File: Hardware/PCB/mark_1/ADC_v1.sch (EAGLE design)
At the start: 1 part, among them Q1 IRLML6402

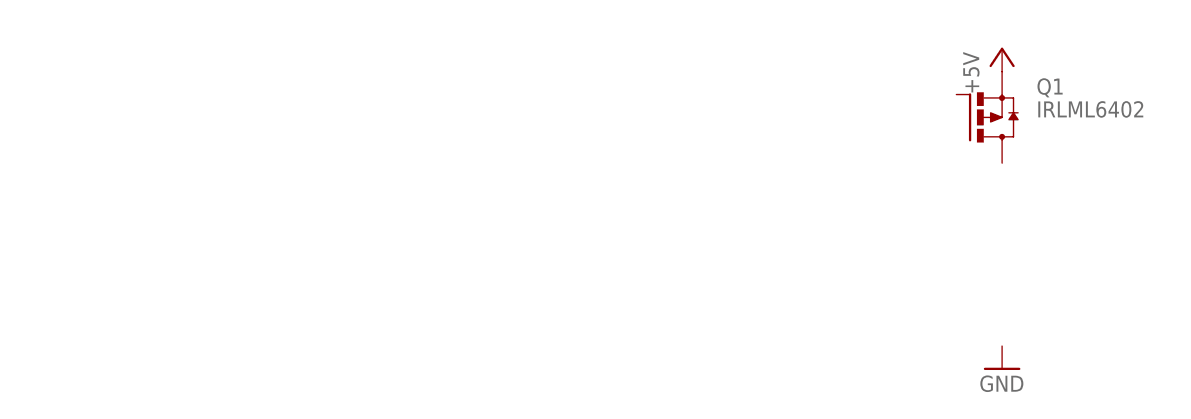
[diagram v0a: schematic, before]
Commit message: 
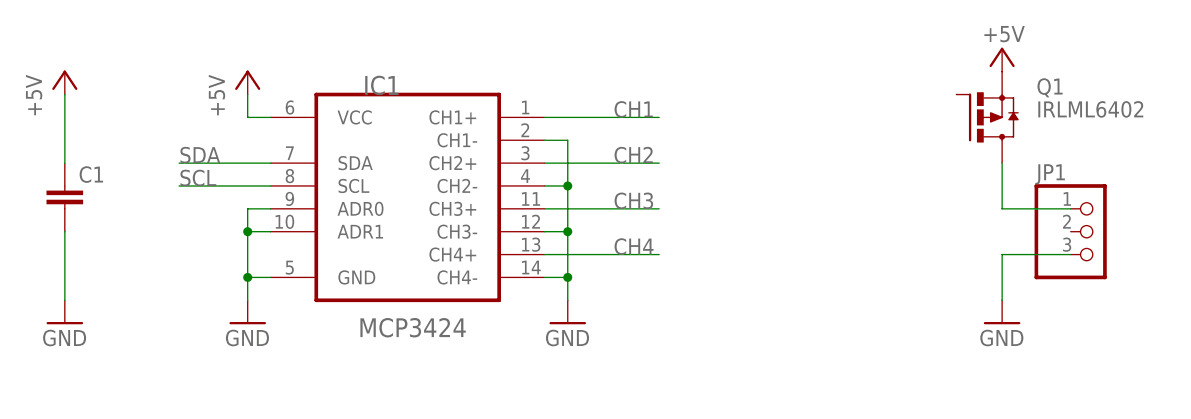
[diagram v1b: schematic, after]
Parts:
- added C1: (no value), mark_1:C-EUC0805K
- added IC1: MCP3424, mark_1:MCP3424
- added JP1: (no value), mark_1:PINHD-1X3180
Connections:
- new net CH1: IC1.CH1+
- new net CH2: IC1.CH2+
- new net CH3: IC1.CH3+
- new net CH4: IC1.CH4+
- new net GND: C1.2, IC1.ADR0, IC1.ADR1, IC1.CH1-, IC1.CH2-, IC1.CH3-, IC1.CH4-, IC1.GND, JP1.3
- new net N$1: JP1.1, Q1.D
- new net SCL: IC1.SCL
- new net SDA: IC1.SDA
- net +5V: now also C1.1, IC1.VCC
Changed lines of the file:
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@@
 <part name="P+1" library="mark_1" deviceset="+5V" device=""/>
 <part name="GND1" library="mark_1" deviceset="GND" device=""/>
+<part name="IC1" library="mark_1" deviceset="MCP3424" device=""/>
+<part name="P+2" library="mark_1" deviceset="+5V" device=""/>
+<part name="GND2" library="mark_1" deviceset="GND" device=""/>
+<part name="C1" library="mark_1" deviceset="C-EU" device="C0805K"/>
+<part name="P+3" library="mark_1" deviceset="+5V" device=""/>
+<part name="GND3" library="mark_1" deviceset="GND" device=""/>
+<part name="JP1" library="mark_1" deviceset="PINHD-1X3" device="180"/>
+<part name="GND4" library="mark_1" deviceset="GND" device=""/>
 </parts>
 <sheets>
@@
 <instances>
 <instance part="Q1" gate="G$1" x="25.4" y="40.64"/>
-<instance part="P+1" gate="1" x="27.94" y="48.26"/>
-<instance part="GND1" gate="1" x="27.94" y="12.7"/>
+<instance part="P+1" gate="1" x="27.94" y="48.26" smashed="yes">
+<attribute name="VALUE" x="30.48" y="50.8" size="1.778" layer="96" rot="R180"/>
+</instance>
+<instance part="GND1" gate="1" x="-20.32" y="17.78"/>
+<instance part="IC1" gate="A" x="-38.1" y="33.02"/>
+<instance part="P+2" gate="1" x="-55.88" y="45.72"/>
+<instance part="GND2" gate="1" x="-55.88" y="17.78"/>
+<instance part="C1" gate="G$1" x="-76.2" y="33.02"/>
+<instance part="P+3" gate="1" x="-76.2" y="45.72"/>
+<instance part="GND3" gate="1" x="-76.2" y="17.78"/>
+<instance part="JP1" gate="A" x="38.1" y="27.94"/>
+<instance part="GND4" gate="1" x="27.94" y="17.78"/>
 </instances>
 <busses>
@@
 <pinref part="P+1" gate="1" pin="+5V"/>
 </segment>
+<segment>
+<pinref part="IC1" gate="A" pin="VCC"/>
+<pinref part="P+2" gate="1" pin="+5V"/>
+<wire x1="-55.88" y1="43.18" x2="-55.88" y2="40.64" width="0.1524" layer="91"/>
+<wire x1="-55.88" y1="40.64" x2="-53.34" y2="40.64" width="0.1524" layer="91"/>
+</segment>
+<segment>
+<pinref part="C1" gate="G$1" pin="1"/>
+<pinref part="P+3" gate="1" pin="+5V"/>
+<wire x1="-76.2" y1="43.18" x2="-76.2" y2="35.56" width="0.1524" layer="91"/>
+</segment>
 </net>
+<net name="GND" class="0">
+<segment>
+<pinref part="IC1" gate="A" pin="GND"/>
+<pinref part="GND2" gate="1" pin="GND"/>
+<wire x1="-55.88" y1="20.32" x2="-55.88" y2="22.86" width="0.1524" layer="91"/>
+<wire x1="-55.88" y1="22.86" x2="-53.34" y2="22.86" width="0.1524" layer="91"/>
+<junction x="-55.88" y="22.86"/>
+<pinref part="IC1" gate="A" pin="ADR0"/>
+<wire x1="-53.34" y1="30.48" x2="-55.88" y2="30.48" width="0.1524" layer="91"/>
+<wire x1="-55.88" y1="30.48" x2="-55.88" y2="27.94" width="0.1524" layer="91"/>
+<junction x="-55.88" y="27.94"/>
+<wire x1="-55.88" y1="27.94" x2="-55.88" y2="22.86" width="0.1524" layer="91"/>
+<pinref part="IC1" gate="A" pin="ADR1"/>
+<wire x1="-53.34" y1="27.94" x2="-55.88" y2="27.94" width="0.1524" layer="91"/>
+</segment>
+<segment>
+<pinref part="IC1" gate="A" pin="CH1-"/>
+<pinref part="GND1" gate="1" pin="GND"/>
+<wire x1="-22.86" y1="38.1" x2="-20.32" y2="38.1" width="0.1524" layer="91"/>
+<wire x1="-20.32" y1="38.1" x2="-20.32" y2="33.02" width="0.1524" layer="91"/>
+<junction x="-20.32" y="22.86"/>
+<wire x1="-20.32" y1="33.02" x2="-20.32" y2="27.94" width="0.1524" layer="91"/>
+<wire x1="-20.32" y1="27.94" x2="-20.32" y2="22.86" width="0.1524" layer="91"/>
+<wire x1="-20.32" y1="22.86" x2="-20.32" y2="20.32" width="0.1524" layer="91"/>
+<junction x="-20.32" y="27.94"/>
+<junction x="-20.32" y="33.02"/>
+<pinref part="IC1" gate="A" pin="CH2-"/>
+<wire x1="-22.86" y1="33.02" x2="-20.32" y2="33.02" width="0.1524" layer="91"/>
+<pinref part="IC1" gate="A" pin="CH3-"/>
+<wire x1="-22.86" y1="27.94" x2="-20.32" y2="27.94" width="0.1524" layer="91"/>
+<pinref part="IC1" gate="A" pin="CH4-"/>
+<wire x1="-22.86" y1="22.86" x2="-20.32" y2="22.86" width="0.1524" layer="91"/>
+</segment>
+<segment>
+<pinref part="C1" gate="G$1" pin="2"/>
+<pinref part="GND3" gate="1" pin="GND"/>
+<wire x1="-76.2" y1="20.32" x2="-76.2" y2="27.94" width="0.1524" layer="91"/>
+</segment>
+<segment>
+<pinref part="JP1" gate="A" pin="3"/>
+<pinref part="GND4" gate="1" pin="GND"/>
+<wire x1="35.56" y1="25.4" x2="27.94" y2="25.4" width="0.1524" layer="91"/>
+<wire x1="27.94" y1="25.4" x2="27.94" y2="20.32" width="0.1524" layer="91"/>
+</segment>
+</net>
+<net name="CH1" class="0">
+<segment>
+<pinref part="IC1" gate="A" pin="CH1+"/>
+<wire x1="-22.86" y1="40.64" x2="-10.16" y2="40.64" width="0.1524" layer="91"/>
+<label x="-15.24" y="40.64" size="1.778" layer="95"/>
+</segment>
+</net>
+<net name="CH2" class="0">
+<segment>
+<pinref part="IC1" gate="A" pin="CH2+"/>
+<wire x1="-22.86" y1="35.56" x2="-10.16" y2="35.56" width="0.1524" layer="91"/>
+<label x="-15.24" y="35.56" size="1.778" layer="95"/>
+</segment>
+</net>
+<net name="CH3" class="0">
+<segment>
+<pinref part="IC1" gate="A" pin="CH3+"/>
+<wire x1="-22.86" y1="30.48" x2="-10.16" y2="30.48" width="0.1524" layer="91"/>
+<label x="-15.24" y="30.48" size="1.778" layer="95"/>
+</segment>
+</net>
+<net name="CH4" class="0">
+<segment>
+<pinref part="IC1" gate="A" pin="CH4+"/>
+<wire x1="-22.86" y1="25.4" x2="-10.16" y2="25.4" width="0.1524" layer="91"/>
+<label x="-15.24" y="25.4" size="1.778" layer="95"/>
+</segment>
+</net>
+<net name="SDA" class="0">
+<segment>
+<pinref part="IC1" gate="A" pin="SDA"/>
+<wire x1="-53.34" y1="35.56" x2="-63.5" y2="35.56" width="0.1524" layer="91"/>
+<label x="-63.5" y="35.56" size="1.778" layer="95"/>
+</segment>
+</net>
+<net name="SCL" class="0">
+<segment>
+<pinref part="IC1" gate="A" pin="SCL"/>
+<wire x1="-53.34" y1="33.02" x2="-63.5" y2="33.02" width="0.1524" layer="91"/>
+<label x="-63.5" y="33.02" size="1.778" layer="95"/>
+</segment>
+</net>
+<net name="N$1" class="0">
+<segment>
+<pinref part="JP1" gate="A" pin="1"/>
+<pinref part="Q1" gate="G$1" pin="D"/>
+<wire x1="35.56" y1="30.48" x2="27.94" y2="30.48" width="0.1524" layer="91"/>
+<wire x1="27.94" y1="30.48" x2="27.94" y2="35.56" width="0.1524" layer="91"/>
+</segment>
+</net>

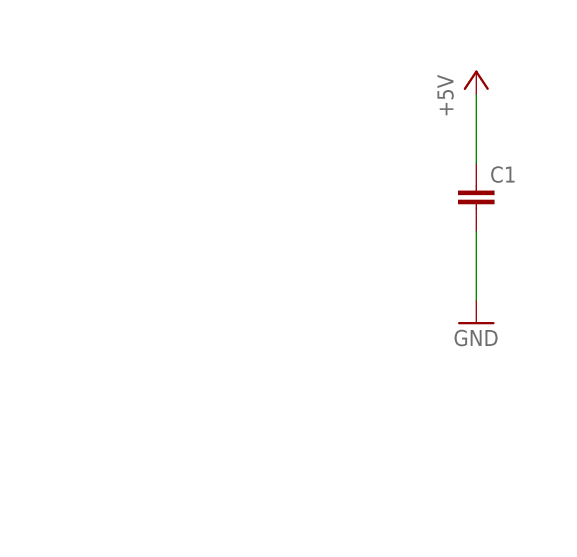
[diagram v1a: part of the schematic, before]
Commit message: 
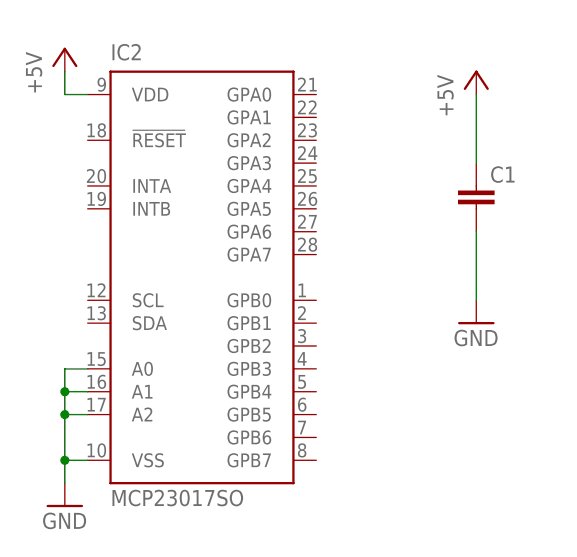
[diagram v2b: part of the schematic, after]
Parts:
- added IC2: MCP23017SO, mark_1:MCP23017SO
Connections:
- net +5V: now also IC2.VDD
- net GND: now also IC2.A0, IC2.A1, IC2.A2, IC2.VSS
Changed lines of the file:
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@@
 <part name="JP1" library="mark_1" deviceset="PINHD-1X3" device="180"/>
 <part name="GND4" library="mark_1" deviceset="GND" device=""/>
+<part name="IC2" library="mark_1" deviceset="MCP23017" device="SO"/>
+<part name="P+4" library="mark_1" deviceset="+5V" device=""/>
+<part name="GND5" library="mark_1" deviceset="GND" device=""/>
 </parts>
 <sheets>
@@
 <instance part="JP1" gate="A" x="38.1" y="27.94"/>
 <instance part="GND4" gate="1" x="27.94" y="17.78"/>
+<instance part="IC2" gate="G$1" x="-106.68" y="22.86"/>
+<instance part="P+4" gate="1" x="-121.92" y="48.26"/>
+<instance part="GND5" gate="1" x="-121.92" y="-2.54"/>
 </instances>
 <busses>
@@
 <pinref part="P+3" gate="1" pin="+5V"/>
 <wire x1="-76.2" y1="43.18" x2="-76.2" y2="35.56" width="0.1524" layer="91"/>
+</segment>
+<segment>
+<pinref part="IC2" gate="G$1" pin="VDD"/>
+<pinref part="P+4" gate="1" pin="+5V"/>
+<wire x1="-121.92" y1="45.72" x2="-121.92" y2="43.18" width="0.1524" layer="91"/>
+<wire x1="-121.92" y1="43.18" x2="-119.38" y2="43.18" width="0.1524" layer="91"/>
 </segment>
 </net>
@@
 <wire x1="27.94" y1="25.4" x2="27.94" y2="20.32" width="0.1524" layer="91"/>
 </segment>
+<segment>
+<pinref part="IC2" gate="G$1" pin="VSS"/>
+<wire x1="-119.38" y1="2.54" x2="-121.92" y2="2.54" width="0.1524" layer="91"/>
+<wire x1="-121.92" y1="2.54" x2="-121.92" y2="0" width="0.1524" layer="91"/>
+<pinref part="GND5" gate="1" pin="GND"/>
+<junction x="-121.92" y="2.54"/>
+<pinref part="IC2" gate="G$1" pin="A0"/>
+<wire x1="-119.38" y1="12.7" x2="-121.92" y2="12.7" width="0.1524" layer="91"/>
+<wire x1="-121.92" y1="12.7" x2="-121.92" y2="10.16" width="0.1524" layer="91"/>
+<junction x="-121.92" y="10.16"/>
+<wire x1="-121.92" y1="10.16" x2="-121.92" y2="7.62" width="0.1524" layer="91"/>
+<junction x="-121.92" y="7.62"/>
+<wire x1="-121.92" y1="7.62" x2="-121.92" y2="2.54" width="0.1524" layer="91"/>
+<pinref part="IC2" gate="G$1" pin="A1"/>
+<wire x1="-119.38" y1="10.16" x2="-121.92" y2="10.16" width="0.1524" layer="91"/>
+<pinref part="IC2" gate="G$1" pin="A2"/>
+<wire x1="-119.38" y1="7.62" x2="-121.92" y2="7.62" width="0.1524" layer="91"/>
+</segment>
 </net>

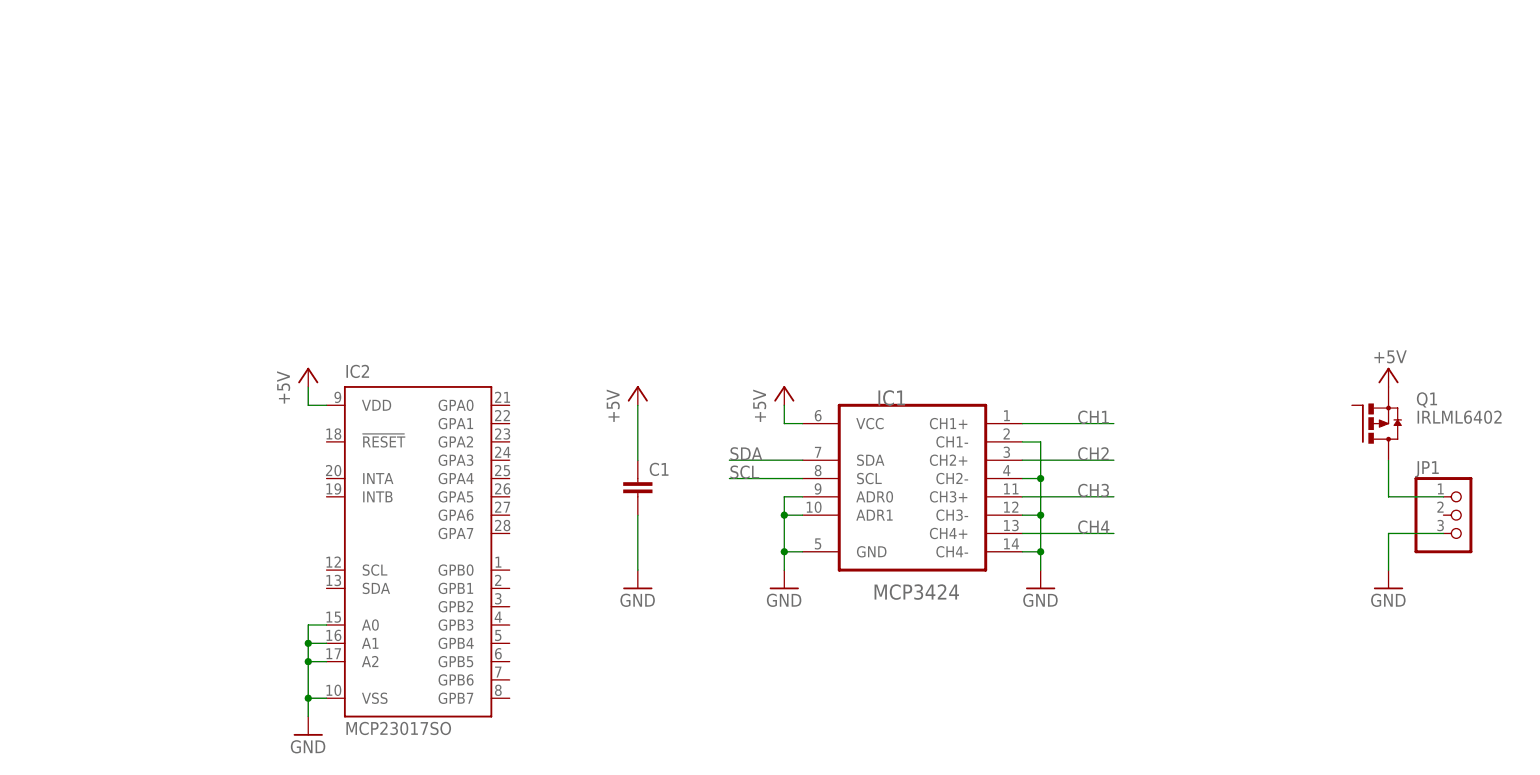
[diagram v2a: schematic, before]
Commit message: 
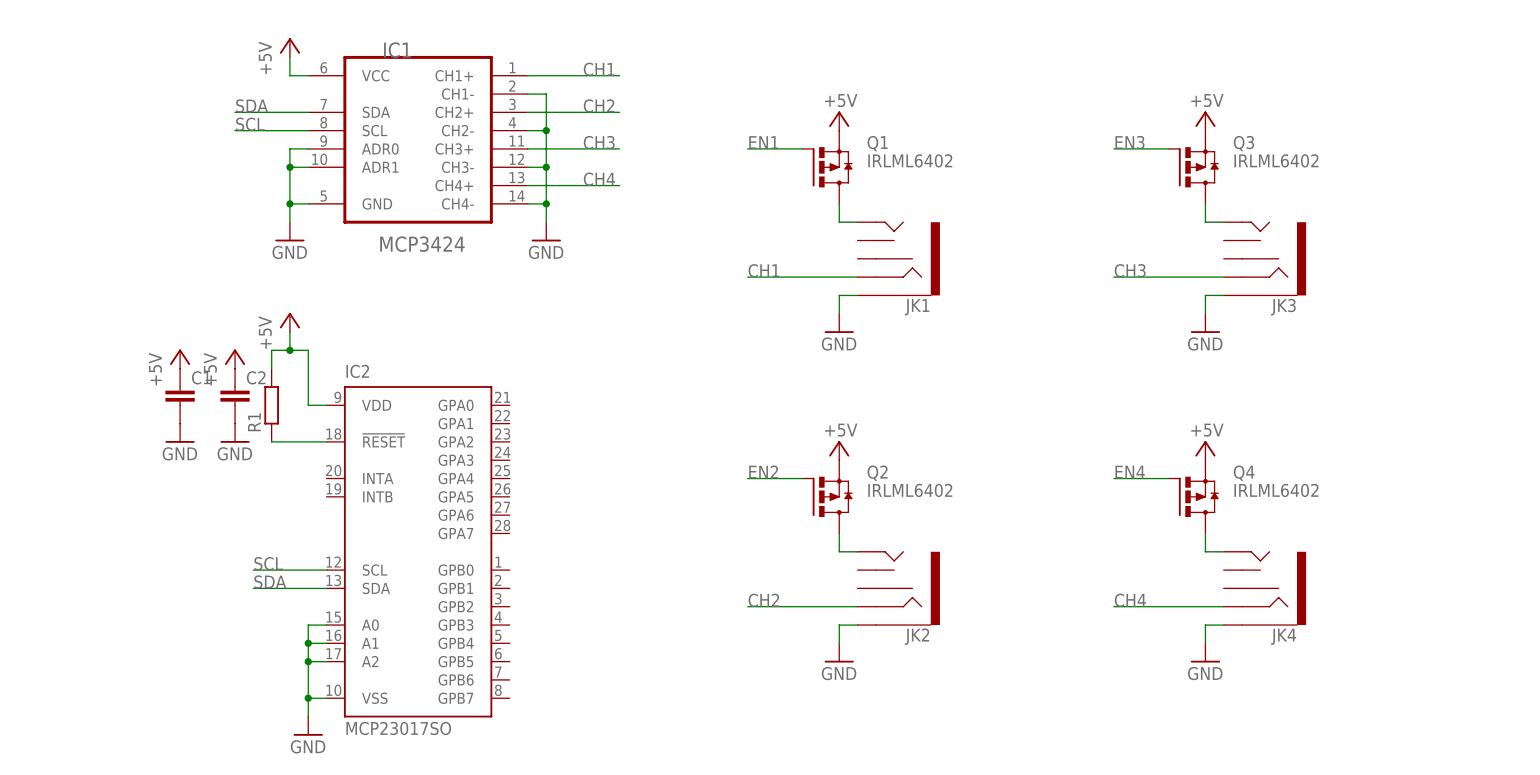
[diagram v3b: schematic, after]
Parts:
- removed JP1: (no value), mark_1:PINHD-1X3180
- added C2: (no value), mark_1:C-EUC0805K
- added JK1, JK2, JK3, JK4: (no value), mark_1:AUDIO-JACK2PTH
- added Q2, Q3, Q4: IRLML6402, mark_1:IRLML6402
- added R1: (no value), mark_1:R-EU_R0805
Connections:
- new net EN1: Q1.G
- new net EN2: Q2.G
- new net EN3: Q3.G
- new net EN4: Q4.G
- new net N$2: IC2.!RESET, R1.1
- new net N$3: JK2.TIP, Q2.D
- new net N$4: JK3.TIP, Q3.D
- new net N$5: JK4.TIP, Q4.D
- net +5V: now also C2.1, Q2.S, Q3.S, Q4.S, R1.2
- net CH1: now also JK1.RING
- net CH2: now also JK2.RING
- net CH3: now also JK3.RING
- net CH4: now also JK4.RING
- net GND: now also C2.2, JK1.SLEEVE, JK2.SLEEVE, JK3.SLEEVE, JK4.SLEEVE; no longer JP1.3
- net N$1: now also JK1.TIP; no longer JP1.1
- net SCL: now also IC2.SCL
- net SDA: now also IC2.SDA
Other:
- moved on the sheet: C1, IC1, Q1
